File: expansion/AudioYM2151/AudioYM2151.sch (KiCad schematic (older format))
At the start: 9 parts, among them J1 D68K_64PIN_BOARD, U1 74LS125, U2 XC95144XL-TQ100

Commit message: YM2151 Initial board placement done
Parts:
- added J4: XilinxJTAG, Connector_PinHeader_2.54mm:PinHeader_2x07_P2.54mm_Vertical, symbol Ddraig:XilinxJTAG
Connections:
- net +3V3: now also J4.2 (VREF)
- net A1: now also U2.34 (P34); no longer U2.11 (P11)
- net A2: now also U2.33 (P33); no longer U2.12 (P12)
- net A3: now also U2.32 (P32); no longer U2.13 (P13)
- net A4: now also U2.30 (P30); no longer U2.14 (P14)
- net A5: now also U2.29 (P29); no longer U2.15 (P15)
- net A6: now also U2.28 (P28); no longer U2.16 (P16)
- net A7: now also U2.27 (I/O/GCK3); no longer U2.17 (P17)
- net CS_DATA: now also U2.8 (P8)
- net CS_REG: now also U2.9 (P9)
- net CS_YMCLK: now also U2.20 (P20)
- net D0: now also U2.59 (P59); no longer U2.35 (P35)
- net D1: now also U2.58 (P58); no longer U2.36 (P36)
- net D10: now also U2.35 (P35); no longer U2.74 (P74)
- net D11: now also U2.36 (P36); no longer U2.76 (P76)
- net D12: now also U2.37 (P37); no longer U2.77 (P77)
- net D13: now also U2.39 (P39); no longer U2.78 (P78)
- net D14: now also U2.40 (P40); no longer U2.79 (P79)
- net D15: now also U2.41 (P41); no longer U2.80 (P80)
- net D2: now also U2.56 (P56); no longer U2.37 (P37)
- net D3: now also U2.55 (P55); no longer U2.39 (P39)
- net D4: now also U2.54 (P54); no longer U2.40 (P40)
- net D5: now also U2.53 (P53); no longer U2.41 (P41)
- net D6: now also U2.52 (P52); no longer U2.42 (P42)
- net D7: now also U2.50 (P50); no longer U2.43 (P43)
- net GND: now also J4.11 (GND), J4.3 (GND), J4.5 (GND), J4.7 (GND), J4.9 (GND)
- net LED: now also U2.66 (P66)
- net OVF: now also U2.96 (P96)
- net PLAYM: now also U2.95 (P95)
- net RECM: now also U2.94 (P94)
- net R~W: now also U2.13 (P13)
- net SPI_CLK: now also U2.18 (P18)
- net SPI_DO: now also U2.19 (P19)
- net ~DTACK: now also U2.16 (P16)
- net ~IRQ: now also U2.14 (P14)
- net ~LDS: now also U2.11 (P11)
- net ~RESET: now also U2.17 (P17)
- net ~UDS: now also U2.12 (P12)
- net ~YM_IRQ: now also U2.93 (P93)
- net ~MSM_RD: now reaches U2.1 (I/O/GTS3)
- net ~MSM_CS: now reaches U2.2 (I/O/GTS4)
- net MSM_CMD: now reaches U2.3 (I/O/GTS1)
- net ADPCM_SIZE: now reaches U2.4 (I/O/GTS2)
- net at U2.45 (TDI): now also J4.10 (TDI)
- net at U2.47 (TMS): now also J4.4 (TMS)
- net at U2.48 (TCK): now also J4.6 (TCK)
- net SAM1: now reaches U2.6 (P6)
- net SAM2: now reaches U2.7 (P7)
- net at U2.83 (TDO): now also J4.8 (TDO)
- net ~CS_YM: now reaches U2.90 (P90)
- net ~RD_YM: now reaches U2.91 (P91)
- net ~WR_YM: now reaches U2.92 (P92)
- net ~MSM_WR: now reaches U2.99 (I/O/GSR)
- new net RECP: U2.15 (P15)
- no-connect marks 19 -> 51

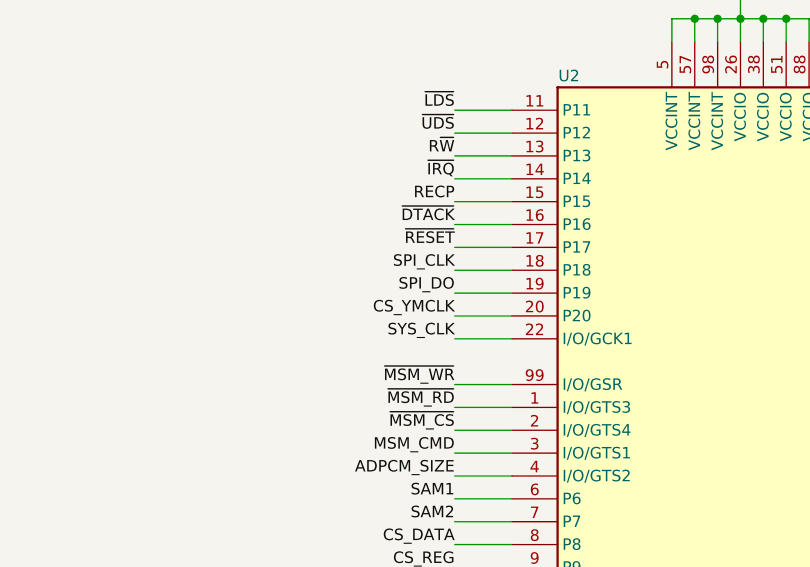
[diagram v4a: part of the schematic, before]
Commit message: Changed POT and some other layout changes
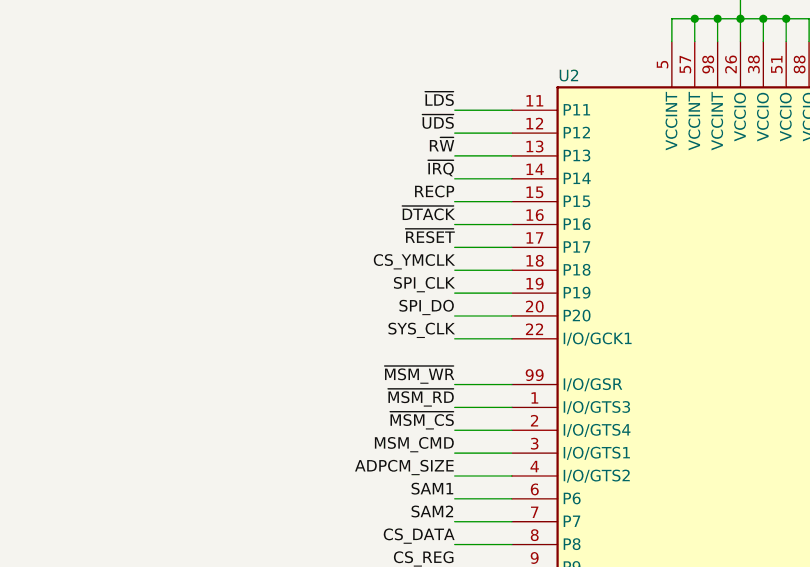
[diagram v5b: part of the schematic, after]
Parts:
- J4: footprint Connector_PinHeader_2.54mm:PinHeader_2x07_P2.54mm_Vertical -> Connector_IDC:IDC-Header_2x07_P2.54mm_Vertical
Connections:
- net CS_YMCLK: now also U2.18 (P18); no longer U2.20 (P20)
- net SPI_CLK: now also U2.19 (P19); no longer U2.18 (P18)
- net SPI_DO: now also U2.20 (P20); no longer U2.19 (P19)
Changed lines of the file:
@@
 F 0 "J4" H 9600 7815 50  0000 C CNN
 F 1 "XilinxJTAG" H 9600 7724 50  0000 C CNN
-F 2 "Connector_PinHeader_2.54mm:PinHeader_2x07_P2.54mm_Vertical" H 9600 7150 50  0001 C CNN
+F 2 "Connector_IDC:IDC-Header_2x07_P2.54mm_Vertical" H 9600 7150 50  0001 C CNN
 F 3 "" H 9600 7150 50  0001 C CNN
 	1    9600 7150
@@
 Wire Wire Line
 	8100 4600 8550 4600
+Text Label 5850 2400 2    50   ~ 0
+SPI_CLK
+Text Label 5850 2500 2    50   ~ 0
+SPI_DO
 Text Label 5850 2300 2    50   ~ 0
-SPI_CLK
-Text Label 5850 2400 2    50   ~ 0
-SPI_DO
-Text Label 5850 2500 2    50   ~ 0
 CS_YMCLK
 Wire Wire Line

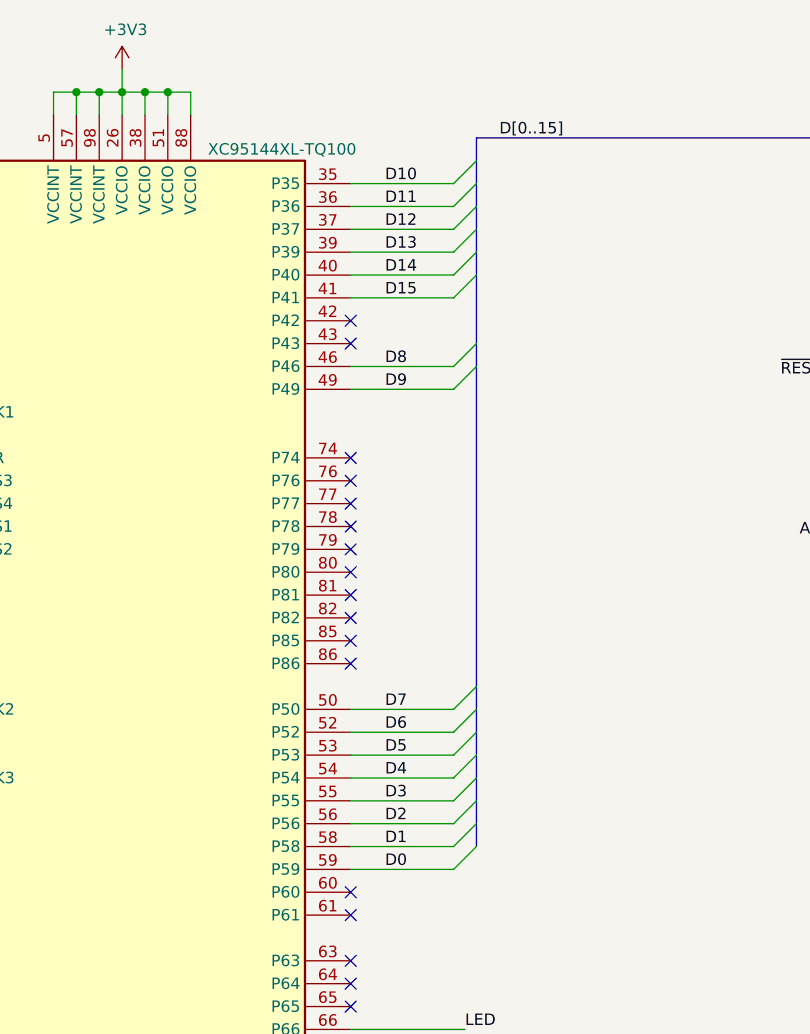
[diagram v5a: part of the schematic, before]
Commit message: Added V9990 IC
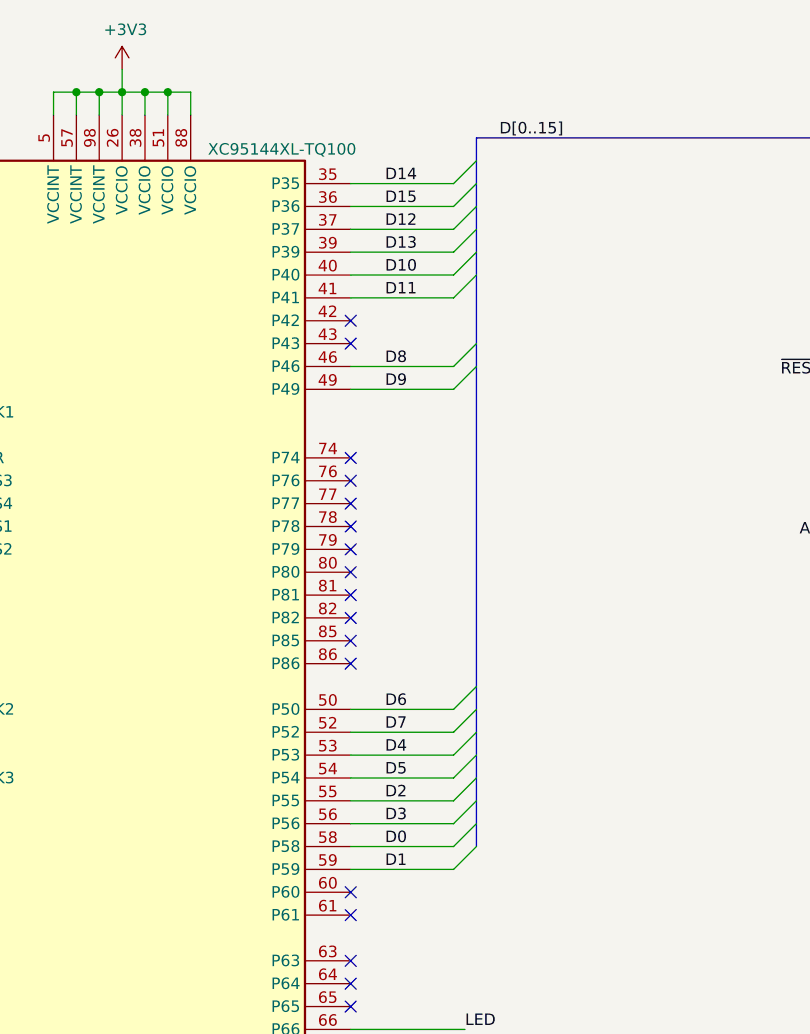
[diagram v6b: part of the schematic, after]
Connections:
- net D0: now also U2.58 (P58); no longer U2.59 (P59)
- net D1: now also U2.59 (P59); no longer U2.58 (P58)
- net D10: now also U2.40 (P40); no longer U2.35 (P35)
- net D11: now also U2.41 (P41); no longer U2.36 (P36)
- net D14: now also U2.35 (P35); no longer U2.40 (P40)
- net D15: now also U2.36 (P36); no longer U2.41 (P41)
- net D2: now also U2.55 (P55); no longer U2.56 (P56)
- net D3: now also U2.56 (P56); no longer U2.55 (P55)
- net D4: now also U2.53 (P53); no longer U2.54 (P54)
- net D5: now also U2.54 (P54); no longer U2.53 (P53)
- net D6: now also U2.50 (P50); no longer U2.52 (P52)
- net D7: now also U2.52 (P52); no longer U2.50 (P50)
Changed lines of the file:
@@
 Wire Wire Line
 	8100 2100 8550 2100
+Text Label 8250 4500 0    50   ~ 0
+D0
 Text Label 8250 4600 0    50   ~ 0
-D0
-Text Label 8250 4500 0    50   ~ 0
 D1
+Text Label 8250 4300 0    50   ~ 0
+D2
 Text Label 8250 4400 0    50   ~ 0
-D2
-Text Label 8250 4300 0    50   ~ 0
 D3
+Text Label 8250 4100 0    50   ~ 0
+D4
 Text Label 8250 4200 0    50   ~ 0
-D4
-Text Label 8250 4100 0    50   ~ 0
 D5
+Text Label 8250 3900 0    50   ~ 0
+D6
 Text Label 8250 4000 0    50   ~ 0
-D6
-Text Label 8250 3900 0    50   ~ 0
 D7
 Text Label 8250 2400 0    50   ~ 0
@@
 Text Label 8250 2500 0    50   ~ 0
 D9
-Text Label 8250 1600 0    50   ~ 0
+Text Label 8250 2000 0    50   ~ 0
 D10
-Text Label 8250 1700 0    50   ~ 0
+Text Label 8250 2100 0    50   ~ 0
 D11
 Text Label 8250 1800 0    50   ~ 0
@@
 Text Label 8250 1900 0    50   ~ 0
 D13
-Text Label 8250 2000 0    50   ~ 0
+Text Label 8250 1600 0    50   ~ 0
 D14
-Text Label 8250 2100 0    50   ~ 0
+Text Label 8250 1700 0    50   ~ 0
 D15
 Text Label 8750 1400 0    50   ~ 0

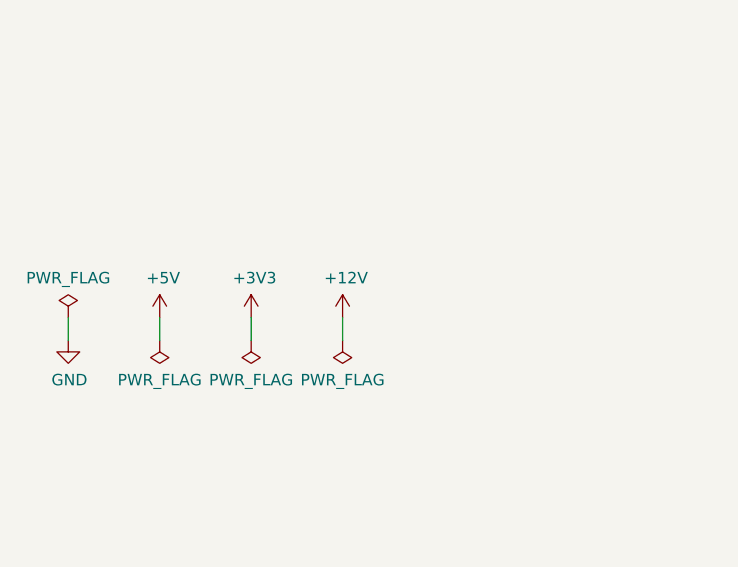
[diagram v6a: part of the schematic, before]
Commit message: Added Eth8019 and updated page description for all projects
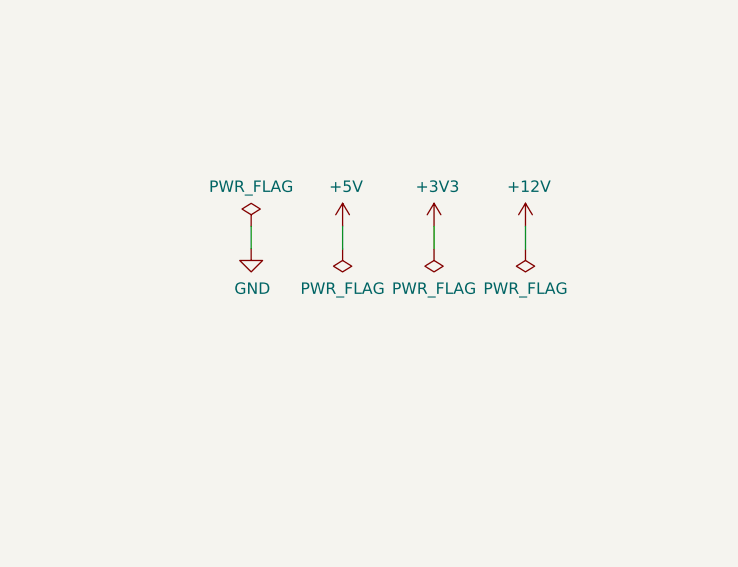
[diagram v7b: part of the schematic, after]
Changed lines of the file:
@@
 L power:GND #PWR0168
 U 1 1 614464E2
-P 1050 4200
-F 0 "#PWR0168" H 1050 3950 50  0001 C CNN
-F 1 "GND" H 1055 4027 50  0000 C CNN
-F 2 "" H 1050 4200 50  0001 C CNN
-F 3 "" H 1050 4200 50  0001 C CNN
-	1    1050 4200
+P 1850 3800
+F 0 "#PWR0168" H 1850 3550 50  0001 C CNN
+F 1 "GND" H 1855 3627 50  0000 C CNN
+F 2 "" H 1850 3800 50  0001 C CNN
+F 3 "" H 1850 3800 50  0001 C CNN
+	1    1850 3800
 	1    0    0    -1
 $EndComp
@@
 L power:+5V #PWR0169
 U 1 1 614468D5
-P 1450 4100
-F 0 "#PWR0169" H 1450 3950 50  0001 C CNN
-F 1 "+5V" H 1465 4273 50  0000 C CNN
-F 2 "" H 1450 4100 50  0001 C CNN
-F 3 "" H 1450 4100 50  0001 C CNN
-	1    1450 4100
+P 2250 3700
+F 0 "#PWR0169" H 2250 3550 50  0001 C CNN
+F 1 "+5V" H 2265 3873 50  0000 C CNN
+F 2 "" H 2250 3700 50  0001 C CNN
+F 3 "" H 2250 3700 50  0001 C CNN
+	1    2250 3700
 	1    0    0    -1
 $EndComp
@@
 L power:+3V3 #PWR0170
 U 1 1 61446E14
-P 1850 4100
-F 0 "#PWR0170" H 1850 3950 50  0001 C CNN
-F 1 "+3V3" H 1865 4273 50  0000 C CNN
-F 2 "" H 1850 4100 50  0001 C CNN
-F 3 "" H 1850 4100 50  0001 C CNN
-	1    1850 4100
+P 2650 3700
+F 0 "#PWR0170" H 2650 3550 50  0001 C CNN
+F 1 "+3V3" H 2665 3873 50  0000 C CNN
+F 2 "" H 2650 3700 50  0001 C CNN
+F 3 "" H 2650 3700 50  0001 C CNN
+	1    2650 3700
 	1    0    0    -1
 $EndComp
@@
 L power:+12V #PWR0171
 U 1 1 61447222
-P 2250 4100
-F 0 "#PWR0171" H 2250 3950 50  0001 C CNN
-F 1 "+12V" H 2265 4273 50  0000 C CNN
-F 2 "" H 2250 4100 50  0001 C CNN
-F 3 "" H 2250 4100 50  0001 C CNN
-	1    2250 4100
+P 3050 3700
+F 0 "#PWR0171" H 3050 3550 50  0001 C CNN
+F 1 "+12V" H 3065 3873 50  0000 C CNN
+F 2 "" H 3050 3700 50  0001 C CNN
+F 3 "" H 3050 3700 50  0001 C CNN
+	1    3050 3700
 	1    0    0    -1
 $EndComp
@@
 L power:PWR_FLAG #FLG0101
 U 1 1 6144822C
-P 1050 4100
-F 0 "#FLG0101" H 1050 4175 50  0001 C CNN
-F 1 "PWR_FLAG" H 1050 4273 50  0000 C CNN
-F 2 "" H 1050 4100 50  0001 C CNN
-F 3 "~" H 1050 4100 50  0001 C CNN
-	1    1050 4100
+P 1850 3700
+F 0 "#FLG0101" H 1850 3775 50  0001 C CNN
+F 1 "PWR_FLAG" H 1850 3873 50  0000 C CNN
+F 2 "" H 1850 3700 50  0001 C CNN
+F 3 "~" H 1850 3700 50  0001 C CNN
+	1    1850 3700
 	1    0    0    -1
 $EndComp
@@
 L power:PWR_FLAG #FLG0102
 U 1 1 61448DBE
-P 1450 4200
-F 0 "#FLG0102" H 1450 4275 50  0001 C CNN
-F 1 "PWR_FLAG" H 1450 4373 50  0000 C CNN
-F 2 "" H 1450 4200 50  0001 C CNN
-F 3 "~" H 1450 4200 50  0001 C CNN
-	1    1450 4200
+P 2250 3800
+F 0 "#FLG0102" H 2250 3875 50  0001 C CNN
+F 1 "PWR_FLAG" H 2250 3973 50  0000 C CNN
+F 2 "" H 2250 3800 50  0001 C CNN
+F 3 "~" H 2250 3800 50  0001 C CNN
+	1    2250 3800
 	-1   0    0    1
 $EndComp
@@
 L power:PWR_FLAG #FLG0103
 U 1 1 61449023
-P 1850 4200
-F 0 "#FLG0103" H 1850 4275 50  0001 C CNN
-F 1 "PWR_FLAG" H 1850 4373 50  0000 C CNN
-F 2 "" H 1850 4200 50  0001 C CNN
-F 3 "~" H 1850 4200 50  0001 C CNN
-	1    1850 4200
+P 2650 3800
+F 0 "#FLG0103" H 2650 3875 50  0001 C CNN
+F 1 "PWR_FLAG" H 2650 3973 50  0000 C CNN
+F 2 "" H 2650 3800 50  0001 C CNN
+F 3 "~" H 2650 3800 50  0001 C CNN
+	1    2650 3800
 	-1   0    0    1
 $EndComp
@@
 L power:PWR_FLAG #FLG0104
 U 1 1 614492B2
-P 2250 4200
-F 0 "#FLG0104" H 2250 4275 50  0001 C CNN
-F 1 "PWR_FLAG" H 2250 4373 50  0000 C CNN
-F 2 "" H 2250 4200 50  0001 C CNN
-F 3 "~" H 2250 4200 50  0001 C CNN
-	1    2250 4200
+P 3050 3800
+F 0 "#FLG0104" H 3050 3875 50  0001 C CNN
+F 1 "PWR_FLAG" H 3050 3973 50  0000 C CNN
+F 2 "" H 3050 3800 50  0001 C CNN
+F 3 "~" H 3050 3800 50  0001 C CNN
+	1    3050 3800
 	-1   0    0    1
 $EndComp
 Wire Wire Line
-	2250 4100 2250 4200
+	3050 3700 3050 3800
 Wire Wire Line
-	1850 4200 1850 4100
+	2650 3800 2650 3700
 Wire Wire Line
-	1450 4100 1450 4200
+	2250 3700 2250 3800
 Wire Wire Line
-	1050 4200 1050 4100
+	1850 3800 1850 3700
 Text Label 10500 4500 2    50   ~ 0
 A1
